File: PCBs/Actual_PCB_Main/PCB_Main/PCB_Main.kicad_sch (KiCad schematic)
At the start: 135 parts, among them J1 LED Connectors+, J10 To_Speaker_R, J2 fan connector, J3 USB_B_Micro, J4 USB_B_Micro, J5 LED connectors -, J6 XT60-M, J7 HUB75, J9 To_Speaker_L, M1 CSD17581Q3, M2 CSD17581Q3A, Q1 S8050, Q2 S8050, Q3 NMOS, Q5 S8050, Q6 S8050, SW1 SW_Push, SW2 SW_Push, SW3 SW_Push, SW4 SW_Push, U1 CP2102N-Axx-xQFN28, U2 AMS1117-3.3, U3 ESP32-WROOM-E, U4 PCM5102A, U5 LM5122MH/NOPB, U6 ESP32-WROVER-E, U7 LM4752TS, U9 CP2102N-Axx-xQFN28, Y1 CB3LV-3I-40M000000, Y2 CB3LV-3I-40M000000

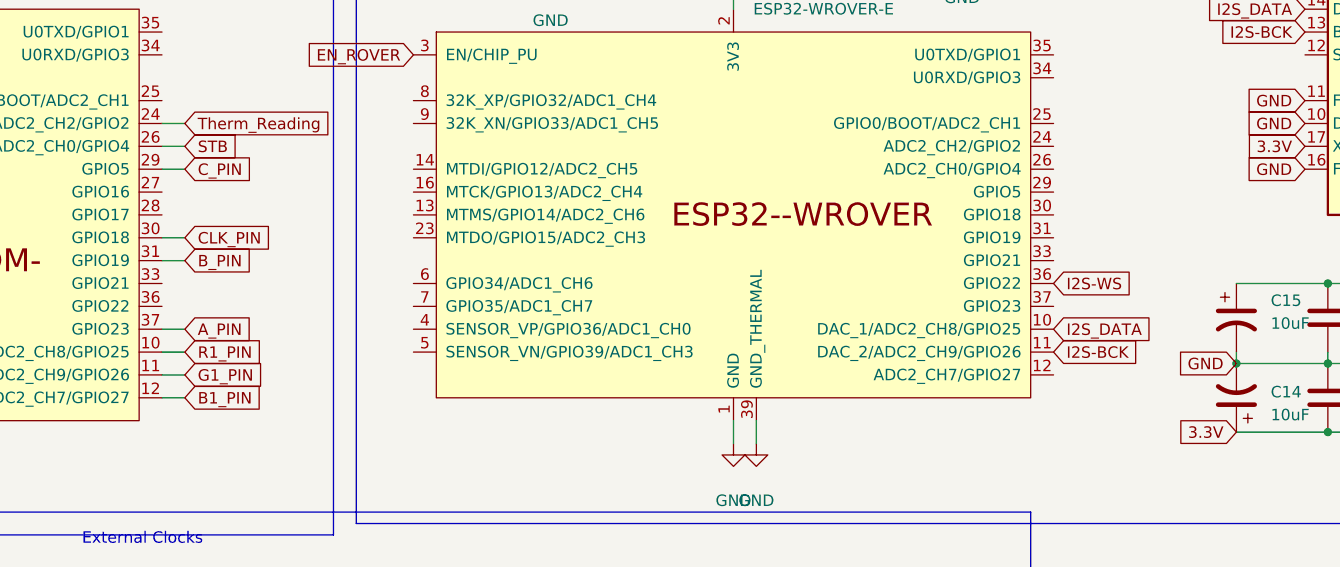
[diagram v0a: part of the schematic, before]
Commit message: Corrected UART receive and transmit pins
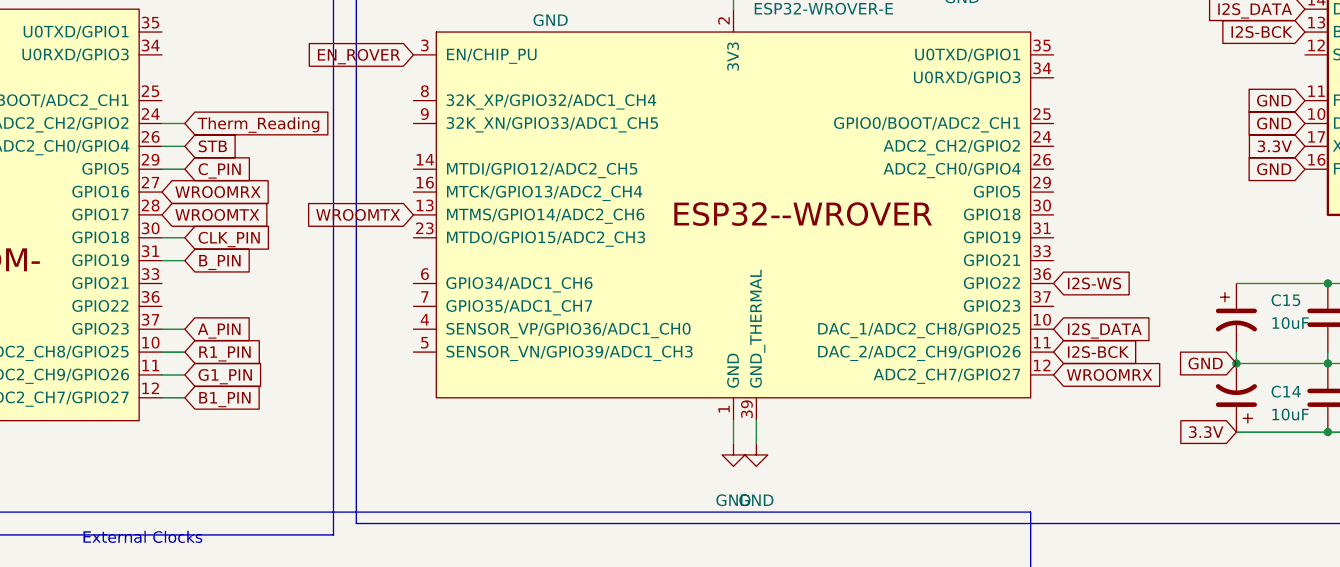
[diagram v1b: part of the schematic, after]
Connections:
- net WROOMRX: now reaches U3.27 (GPIO16)
- net WROOMRX: now also U6.12 (ADC2_CH7/GPIO27)
- net WROOMTX: now reaches U3.28 (GPIO17)
- net WROOMTX: now also U6.13 (MTMS/GPIO14/ADC2_CH6)
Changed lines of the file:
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@@
+    )
+  )
+  (global_label "WROOMTX" (shape input) (at 123.19 109.22 180) (fields_autoplaced)
+    (effects (font (size 1.27 1.27)) (justify right))
+    (property "Intersheetrefs" "${INTERSHEET_REFS}" (at 111.1939 109.22 0)
+      (effects (font (size 1.27 1.27)) (justify right) hide)
     )
   )
@@
     )
   )
+  (global_label "WROOMRX" (shape input) (at 95.25 106.68 0) (fields_autoplaced)
+    (effects (font (size 1.27 1.27)) (justify left))
+    (property "Intersheetrefs" "${INTERSHEET_REFS}" (at 107.5485 106.68 0)
+      (effects (font (size 1.27 1.27)) (justify left) hide)
+    )
+  )
   (global_label "5V" (shape input) (at 29.21 21.59 0) (fields_autoplaced)
     (effects (font (size 1.27 1.27)) (justify left))
@@
     )
   )
+  (global_label "WROOMTX" (shape input) (at 95.25 109.22 0) (fields_autoplaced)
+    (effects (font (size 1.27 1.27)) (justify left))
+    (property "Intersheetrefs" "${INTERSHEET_REFS}" (at 107.2461 109.22 0)
+      (effects (font (size 1.27 1.27)) (justify left) hide)
+    )
+  )
+  (global_label "WROOMRX" (shape input) (at 194.31 127 0) (fields_autoplaced)
+    (effects (font (size 1.27 1.27)) (justify left))
+    (property "Intersheetrefs" "${INTERSHEET_REFS}" (at 206.6085 127 0)
+      (effects (font (size 1.27 1.27)) (justify left) hide)
+    )
+  )

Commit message: BOOT
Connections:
- net IO0_ROVER: now also U6.25 (GPIO0/BOOT/ADC2_CH1)
- net IO0_WROOM: now also U3.25 (GPIO0/BOOT/ADC2_CH1)
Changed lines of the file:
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@@
+    )
+  )
+  (global_label "IO0_ROVER" (shape input) (at 194.31 99.06 0) (fields_autoplaced)
+    (effects (font (size 1.27 1.27)) (justify left))
+    (property "Intersheetrefs" "${INTERSHEET_REFS}" (at 207.5157 99.06 0)
+      (effects (font (size 1.27 1.27)) (justify left) hide)
     )
   )
@@
       (effects (font (size 1.27 1.27)) (justify left) hide)
     )
+  )
+  (global_label "IO0_WROOM" (shape input) (at 95.25 96.52 0) (fields_autoplaced)
+    (effects (font (size 1.27 1.27)) (justify left))
+    (property "Intersheetrefs" "${INTERSHEET_REFS}" (at 109.1814 96.52 0)
+      (effects (font (size 1.27 1.27)) (justify left) hide)
+    )

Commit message: finished schematic
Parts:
- removed D10, D11, D12, D13, D2, D3, D4, D5: BZX84Cxx, Package_TO_SOT_SMD:SOT-23, symbol Diode:BZX84Cxx
- removed D6: RED LED, LED_SMD:LED_0805_2012Metric, symbol Device:LED
- removed J1: LED Connectors+, symbol Connector:Conn_01x03_Pin
- removed J2: fan connector, symbol Connector:Conn_01x02_Pin
- removed J3, J4: USB_B_Micro, symbol Connector:USB_B_Micro
- removed J5: LED connectors -, symbol Connector:Conn_01x03_Pin
- removed Q3: NMOS, symbol Simulation_SPICE:NMOS
- added Boot2ROVER1, Boot2WROOM1: ~, Artisyn_Components:USB_TO_TTL_FT232RL, symbol Interface:USB_TO_TTL_FT232RL
- added C30: 10uF, Capacitor_SMD:C_0805_2012Metric, symbol Device:C
- added C34, CsnR2, CsnR3: .1uF, Capacitor_SMD:C_0805_2012Metric, symbol Device:C
- added D10, D11, D12, D13, D14, D6, D8, D9: MM5Zxx, Diode_SMD:D_SOD-523, symbol Diode:MM5Zxx
- added D7: RED LED, LED_SMD:LED_0805_2012Metric, symbol Device:LED
- added H1, H2, H3, H4: MountingHole, MountingHole:MountingHole_2.7mm, symbol Mechanical:MountingHole
- added J1: fan connector, Connector_PinHeader_2.54mm:PinHeader_1x02_P2.54mm_Vertical, symbol Connector:Conn_01x02_Pin
- added J2, J4: 10118193-0001LF, Artisyn_Components:Artysin_USB_CONN, symbol Artysin_USB_CONN:10118193-0001LF
- added Q4: Fan_NMOS, Artisyn_Components:Fan_MOSFET, symbol Fan_MOSFET:SI1902CDL-T1-BE3
- added R20: 1k, Resistor_SMD:R_0815_2038Metric, symbol Device:R
- added R21: 500, Resistor_SMD:R_0805_2012Metric, symbol Device:R
- C1: value 22uF -> 10uF
- C2: value 22uF -> .1uF
- C25, C26, C27, C29: footprint (none) -> Capacitor_SMD:C_0805_2012Metric
- R19: value 1k -> 500; footprint (none) -> Resistor_SMD:R_0805_2012Metric
- Y1, Y2: footprint CB3LV-3I-40M000000:OSC_CB3LV-3I-40M000000 -> Artisyn_Components:Onboard_Clock
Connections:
- net 3.3V: now also Boot2ROVER1.4 (VCC), Boot2WROOM1.4 (VCC), C30.1, CsnR2.1, CsnR3.1
- net GND: now also Csc1.2, Boot2ROVER1.6 (GND), Boot2WROOM1.6 (GND), C30.2, C34.2, CsnR2.2, CsnR3.2, D11.2 (A), D12.2 (A), D13.2 (A), D6.2 (A), D8.2 (A), D9.2 (A), J2.5 (GND), J4.5 (GND), R20.2; no longer R19.2
- net RXD_ROVER: now also U6.34 (U0RXD/GPIO3), Boot2ROVER1.2 (RX)
- net RXD_WROOM: now also U3.35 (U0TXD/GPIO1), Boot2WROOM1.2 (RX)
- net TXD_ROVER: now also U6.35 (U0TXD/GPIO1), Boot2ROVER1.3 (TX)
- net TXD_WROOM: now also U3.34 (U0RXD/GPIO3), Boot2WROOM1.3 (TX)
- net USB_DN_ROVER: now also D8.1 (K)
- net USB_DN_WROOM: now also D12.1 (K)
- net USB_DP_ROVER: now also D9.1 (K)
- net USB_DP_WROOM: now also D13.1 (K)
- net VBUS_ROVER: now also D14.2 (A), D6.1 (K)
- net VBUS_WROOM: now also D10.2 (A), D11.1 (K)
- net VCC: now also C34.1, D10.1 (K), D14.1 (K), J1.2 (Pin_2)
- net WROOM_TO_FANS: now also U3.7 (GPIO35/ADC1_CH7), Q4.5 (G2)
- net at Cout1.1, Coutx1.1, Csc1.1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: now also C3b1.1
- net at R33.1: now also J4.2 (D-)
- net WROOM_TALK_RX: now reaches R19.1
- net WROOM_TALK_RX: now also U3.27 (GPIO16)
- net at R34.1: now also J4.3 (D+)
- net at R32.1: now also J4.1 (VUSB)
- net at R11.1: now also J2.2 (D-)
- net at R14.1: now also J2.1 (VUSB)
- net at R12.1: now also J2.3 (D+)
- net WROOMRX renamed ROVER_TALK_TX
- net ROVER_TALK_TX: now also R19.2; no longer U3.27 (GPIO16)
- net WROOMTX renamed ROVER_TALK_RX
- net ROVER_TALK_RX: now also R21.2; no longer U3.28 (GPIO17)
- new net: J1.1 (Pin_1), Q4.3 (D2)
- new net: D7.2 (A), Q4.4 (S2)
- new net: D7.1 (K), R20.1
- new net WROOM_TALK_TX: R21.1, U3.28 (GPIO17)
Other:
- note removed: "LED CONNECTORS"
- moved on the sheet: C10, C11, C12, C13, C14, C15, C16, C17, C18, C19, C2, C20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

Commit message: finished Schematic spread PCB compnets for footprint compare
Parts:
- C17, C18: value 2.2uF -> 2.2nF
- C25, C27: value .1uF -> .01uF
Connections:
- net CLK is gone; now on net CLK_PIN: J7.13 (Pin_13)
- net B2_PIN: now also J7.7 (Pin_7); no longer J7.6 (Pin_6)
- net G2_PIN: now also J7.6 (Pin_6); no longer J7.7 (Pin_7)
- net GND: now also J2.S1 (SHIELD), J2.S2 (SHIELD__1), J2.S3 (SHIELD__2), J2.S4 (SHIELD__3), J2.S5 (SHIELD__4), J2.S6 (SHIELD__5), J4.S1 (SHIELD), J4.S2 (SHIELD__1), J4.S3 (SHIELD__2), J4.S4 (SHIELD__3), J4.S5 (SHIELD__4), J4.S6 (SHIELD__5); no longer C13.2, C16.2, C17.2, C18.2, C19.2, C20.1, C21.1, U4.3 (CPGND), U4.9 (AGND)
- net RXD0_ROVER: now also Boot2ROVER1.2 (RX), U6.34 (U0RXD/GPIO3)
- net RXD0_WROOM: now also Boot2WROOM1.2 (RX), U3.34 (U0RXD/GPIO3)
- net RXD_ROVER: no longer Boot2ROVER1.2 (RX), U6.34 (U0RXD/GPIO3)
- net RXD_WROOM: no longer Boot2WROOM1.2 (RX), U3.35 (U0TXD/GPIO1)
- net TXD0_ROVER: now also Boot2ROVER1.3 (TX), U6.35 (U0TXD/GPIO1)
- net TXD0_WROOM: now also Boot2WROOM1.3 (TX), U3.35 (U0TXD/GPIO1)
- net TXD_ROVER: no longer Boot2ROVER1.3 (TX), U6.35 (U0TXD/GPIO1)
- net TXD_WROOM: no longer Boot2WROOM1.3 (TX), U3.34 (U0RXD/GPIO3)
- net WIO21: now reaches U3.33 (GPIO21)
- net WIO22: now reaches U3.36 (GPIO22)
- net WIO39: now reaches U3.5 (SENSOR_VN/GPIO39/ADC1_CH3)
- net WIO34: now reaches U3.6 (GPIO34/ADC1_CH6)
- net WIO32: now reaches U3.8 (32K_XP/GPIO32/ADC1_CH4)
- net RIO12: now reaches U6.14 (MTDI/GPIO12/ADC2_CH5)
- net RIO13: now reaches U6.16 (MTCK/GPIO13/ADC2_CH4)
- net RIO15: now reaches U6.23 (MTDO/GPIO15/ADC2_CH3)
- net RIO2: now reaches U6.24 (ADC2_CH2/GPIO2)
- net RIO4: now reaches U6.26 (ADC2_CH0/GPIO4)
- net RIO5: now reaches U6.29 (GPIO5)
- net RIO18: now reaches U6.30 (GPIO18)
- net RIO19: now reaches U6.31 (GPIO19)
- net RIO21: now reaches U6.33 (GPIO21)
- net RIO23: now reaches U6.37 (GPIO23)
- net RIO36: now reaches U6.4 (SENSOR_VP/GPIO36/ADC1_CH0)
- net RIO39: now reaches U6.5 (SENSOR_VN/GPIO39/ADC1_CH3)
- net RIO34: now reaches U6.6 (GPIO34/ADC1_CH6)
- net RIO35: now reaches U6.7 (GPIO35/ADC1_CH7)
- net RIO32: now reaches U6.8 (32K_XP/GPIO32/ADC1_CH4)
- net RIO33: now reaches U6.9 (32K_XN/GPIO33/ADC1_CH5)
- new net AGND: C13.2, C16.2, C17.2, C18.2, C19.2, C20.1, C21.1, U4.3 (CPGND), U4.9 (AGND)

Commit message: started PCB Layout
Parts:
- R20: footprint Resistor_SMD:R_0815_2038Metric -> Resistor_SMD:R_0805_2012Metric
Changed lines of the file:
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@@
       (effects (font (size 1.27 1.27)) (justify left))
     )
-    (property "Footprint" "Resistor_SMD:R_0815_2038Metric" (at 253.492 34.29 90)
+    (property "Footprint" "Resistor_SMD:R_0805_2012Metric" (at 253.492 34.29 90)
       (effects (font (size 1.27 1.27)) hide)
     )

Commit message: PCB reset traces
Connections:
- net VCC: now also Rsense1.1; no longer Rsense1.2
- net at L1.1, U5.3 (CSN): now also Rsense1.2; no longer Rsense1.1
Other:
- moved on the sheet: Rsense1
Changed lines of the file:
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@@
     )
   )
-  (symbol (lib_id "Device:R") (at 50.8 -74.93 270) (unit 1)
-    (in_bom yes) (on_board yes) (dnp no) (fields_autoplaced)
+  (symbol (lib_id "Device:R") (at 50.8 -74.93 90) (mirror x) (unit 1)
+    (in_bom yes) (on_board yes) (dnp no)
     (property "Reference" "Rsense1" (at 50.8 -81.28 90)
       (effects (font (size 1.27 1.27)))
@@
   )
   (symbol (lib_id "power:GND") (at 316.23 87.63 0) (unit 1)
-    (in_bom yes) (on_board yes) (dnp no) (fields_autoplaced)
+    (in_bom yes) (on_board yes) (dnp no)
     (property "Reference" "#PWR09" (at 316.23 93.98 0)
       (effects (font (size 1.27 1.27)) hide)

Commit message: Add files via upload
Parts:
- added C35: 1000uF, Artisyn_Components:EX_DAC_ELEC_CAPS_10uF, symbol Device:C_Polarized_US
- added R22, R23, R24, R25: 0, Resistor_SMD:R_0805_2012Metric, symbol Device:R
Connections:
- net VCC is gone; now on net GND: C1.1, C34.1, Cin1.1, D10.1 (K), D14.1 (K), J1.2 (Pin_2), J6.P (POS), R10.1, Rsense1.1, Ruvt1.1, Rvin1.1, U2.3 (VI), U5.4 (CSP)
- net GND: now also C35.1, C35.2
- net RXD0_ROVER: now also R24.1; no longer Boot2ROVER1.2 (RX)
- net RXD0_WROOM: now also R22.1; no longer Boot2WROOM1.2 (RX)
- net TXD0_ROVER: now also R25.1; no longer Boot2ROVER1.3 (TX)
- net TXD0_WROOM: now also R23.1; no longer Boot2WROOM1.3 (TX)
- new net: Boot2WROOM1.3 (TX), R23.2
- new net: Boot2ROVER1.3 (TX), R25.2
- new net: Boot2ROVER1.2 (RX), R24.2
- new net: Boot2WROOM1.2 (RX), R22.2
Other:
- moved on the sheet: CsnR2, CsnR3

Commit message: fixed footprints
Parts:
- C35: footprint Artisyn_Components:EX_DAC_ELEC_CAPS_10uF -> Artisyn_Components:Audio_1000uF
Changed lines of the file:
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@@
       (effects (font (size 1.27 1.27)) (justify left))
     )
-    (property "Footprint" "Artisyn_Components:EX_DAC_ELEC_CAPS_10uF" (at 25.4 30.48 0)
+    (property "Footprint" "Artisyn_Components:Audio_1000uF" (at 25.4 30.48 0)
       (effects (font (size 1.27 1.27)) hide)
     )
